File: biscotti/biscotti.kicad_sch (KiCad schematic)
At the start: 5 parts, among them U1 LAN8720A

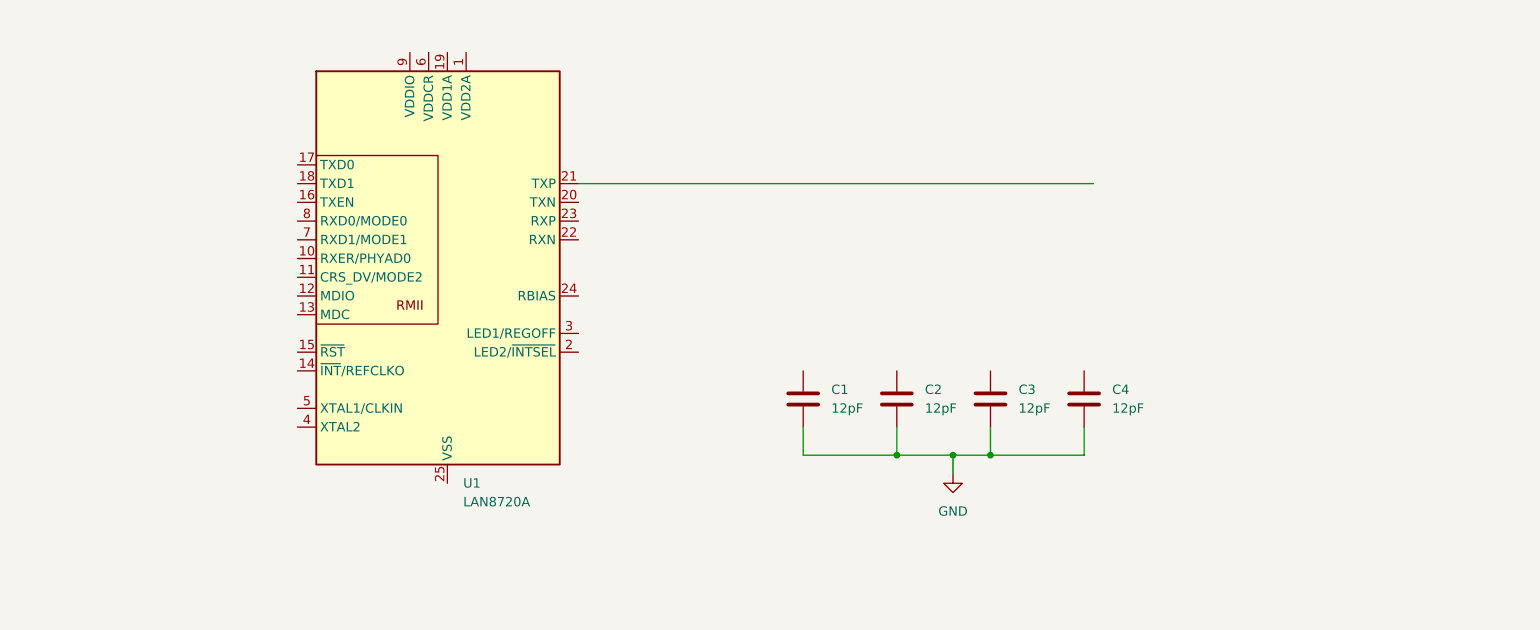
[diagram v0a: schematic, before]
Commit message: wip, started connected configs for LED1/2
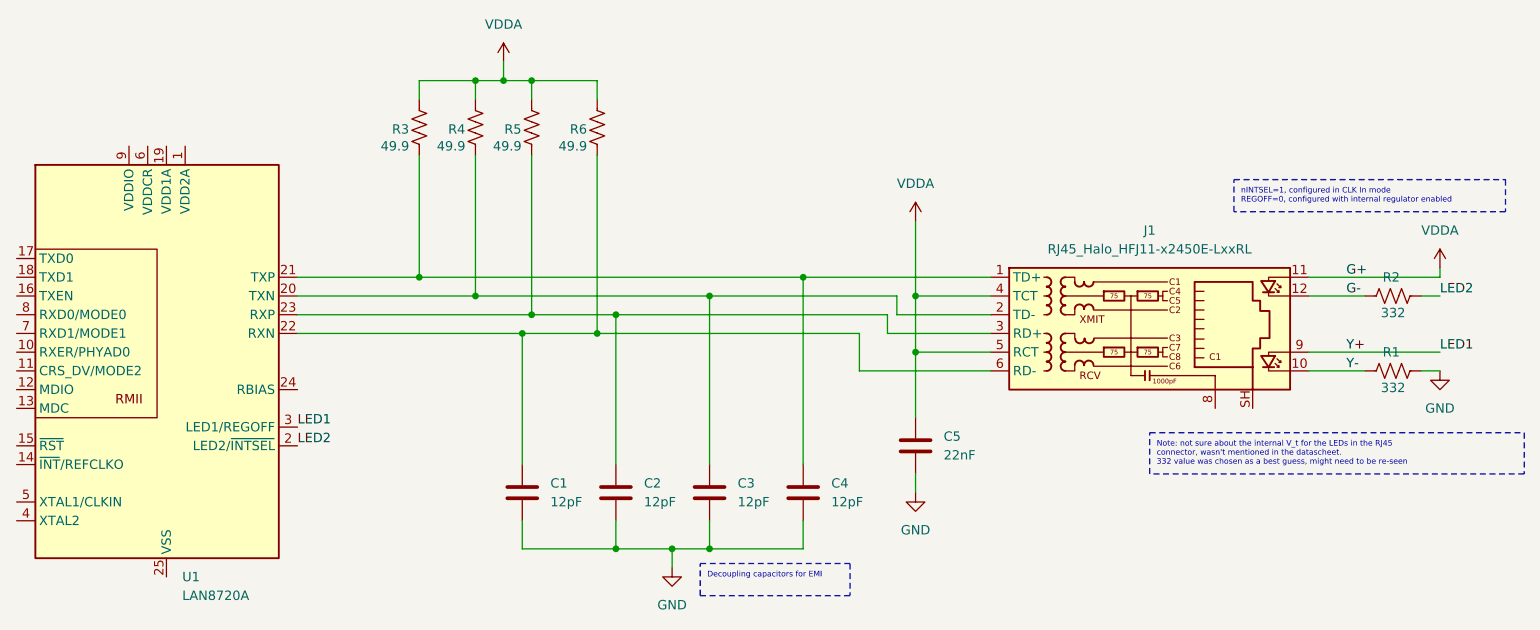
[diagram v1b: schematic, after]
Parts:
- added C5: 22nF, symbol Device:C
- added J1: RJ45_Halo_HFJ11-x2450E-LxxRL, Connector_RJ:RJ45_HALO_HFJ11-x2450E-LxxRL_Horizontal, symbol Connector:RJ45_Halo_HFJ11-x2450E-LxxRL
- added R1, R2: 332, symbol Device:R_US
- added R3, R4, R5, R6: 49.9, symbol Device:R_US
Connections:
- net GND: now also C5.2, R1.1
- net at C3.1: now also U1.20 (TXN), J1.2 (TD-), R4.2
- net at C1.1: now also U1.22 (RXN), J1.6 (RD-), R6.2
- net at C2.1: now also U1.23 (RXP), J1.3 (RD+), R5.2
- net at C4.1: now also U1.21 (TXP), J1.1 (TD+), R3.2
- net LED2: now reaches U1.2 (LED2/~{INTSEL})
- net LED2: now also R2.1
- net LED1: now reaches U1.3 (LED1/REGOFF)
- net LED1: now also J1.9
- new net G-: J1.12, R2.2
- new net VDDA: C5.1, J1.11, J1.4 (TCT), J1.5 (RCT), R3.1, R4.1, R5.1, R6.1
- new net Y-: J1.10, R1.2
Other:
- moved on the sheet: C1, C2, C3, C4, U1

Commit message: wip
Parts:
- added C6: 0.1uF, symbol Device:C
- added J2: Conn_02x06_Top_Bottom, symbol Connector_Generic:Conn_02x06_Top_Bottom
- added J3: Conn_02x01, symbol Connector_Generic:Conn_02x01
- added R7: 12.1k, symbol Device:R_US
- added R8: 1.5k, symbol Device:R_US
- added R9: 4.7k, symbol Device:R_US
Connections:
- net GND: now also U1.25 (VSS), C6.2, R7.2
- net MDIO: now reaches U1.12 (MDIO)
- net MDIO: now also J3.1 (Pin_1), R8.2
- net MDC: now reaches U1.13 (MDC)
- net MDC: now also J3.2 (Pin_2)
- net nRST: now reaches U1.15 (~{RST})
- net nRST: now also C6.1, R9.2
- net at U1.24 (RBIAS): now also R7.1
- net EGND: now reaches J1.8
- net EGND: now also J1.SH
- new net VDD: R8.1, R9.1
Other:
- note added: "EGND: copper pour around RJ45"
- note added: "This pin requires connection of a 12.1k ohm (1%) resistor to ground."

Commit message: add pmod
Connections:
- net GND: now also J2.11 (Pin_11), J2.5 (Pin_5)
- net Clk: now reaches J2.1 (Pin_1)
- net RXD[1]: now reaches J2.10 (Pin_10)
- net 3V3: now reaches J2.12 (Pin_12)
- net 3V3: now also J2.6 (Pin_6)
- net TXV: now reaches J2.2 (Pin_2)
- net RXV: now reaches J2.3 (Pin_3)
- net RXERR: now reaches J2.4 (Pin_4)
- net TXD[0]: now reaches J2.7 (Pin_7)
- net TXD[1]: now reaches J2.8 (Pin_8)
- net RXD[0]: now reaches J2.9 (Pin_9)

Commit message: config modes
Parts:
- added R10, R11, R12, R13: 4.7k, symbol Device:R_US
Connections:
- net GND: now also R12.2, R13.2
- net RXD[0]: now also U1.8 (RXD0/MODE0), R10.2
- net RXD[1]: now also U1.7 (RXD1/MODE1), R11.2
- net RXERR: now also U1.10 (RXER/PHYAD0), R13.1
- net RXV: now also U1.11 (CRS_DV/MODE2), R12.1
- net VDD: now also R10.1, R11.1
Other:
- note added: "MODE[2:0] = 011 100Base-TX Full Duplex. Auto-negotiation disabled. CRS is active during Receive MODE[0] 1 = RXD0/MODE0 MODE[1] 1 = RXD1/MODE1 MODE[2] 0 = CRS_DV/MODE2"

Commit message: finishing schematics and bom, next is routing
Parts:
- added C10, C12, C13, C7: 1uF, symbol Device:C
- added C11, C8, C9: 0.1uF, symbol Device:C
- added C14: 470pF, symbol Device:C
- added FB1: FerriteBead, symbol Device:FerriteBead
- added J4: Conn_01x01, symbol Connector_Generic:Conn_01x01
- added R14, R15, R16, R17: 10, symbol Device:R_US
- added R18: 4.7k, symbol Device:R_US
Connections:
- net Clk: now also U1.5 (XTAL1/CLKIN)
- net GND: now also C10.2, C11.2, C12.2, C13.2, C14.2, C7.2, C8.2, C9.2
- net RXD[0]: now also R14.1; no longer R10.2, U1.8 (RXD0/MODE0)
- net RXD[1]: now also R15.1; no longer R11.2, U1.7 (RXD1/MODE1)
- net RXERR: now also R16.1; no longer R13.1, U1.10 (RXER/PHYAD0)
- net RXV: now also R17.1; no longer R12.1, U1.11 (CRS_DV/MODE2)
- net TXD[0]: now also U1.17 (TXD0)
- net TXD[1]: now also U1.18 (TXD1)
- net TXV: now also U1.16 (TXEN)
- net VDD: now also U1.9 (VDDIO), C10.1, C9.1, FB1.2, R18.1
- net VDDA: now also U1.1 (VDD2A), U1.19 (VDD1A), C11.1, C12.1, C7.1, C8.1, FB1.1
- net nINT: now reaches U1.14 (~{INT}/REFCLKO)
- net nINT: now also J4.1 (Pin_1), R18.2
- net VDDCR: now reaches U1.6 (VDDCR)
- net VDDCR: now also C13.1, C14.1
- new net: R12.1, R17.2, U1.11 (CRS_DV/MODE2)
- new net: R10.2, R14.2, U1.8 (RXD0/MODE0)
- new net: R11.2, R15.2, U1.7 (RXD1/MODE1)
- new net: R13.1, R16.2, U1.10 (RXER/PHYAD0)
- no-connect marks 0 -> 1
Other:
- note added: "Bypass capacitors"
- note added: "nINT, interup, active low, exposed for debug"
- note added: "project_clk already has a 47 ohm resistor in series with the rpi pin (clock gen), so there is no need to add any more Rs on the line"
- moved on the sheet: C6, R12, R13, R9

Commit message: assign all footprints
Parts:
- C1, C10, C11, C12, C13, C14, C2, C3, C4, C5, C6, C7, C8, C9: footprint (none) -> Capacitor_SMD:C_1206_3216Metric_Pad1.33x1.80mm_HandSolder
- FB1: footprint (none) -> Inductor_SMD:L_1206_3216Metric_Pad1.22x1.90mm_HandSolder
- J2: footprint (none) -> Connector_PinHeader_2.54mm:PinHeader_2x06_P2.54mm_Horizontal
- J3: footprint (none) -> Connector_PinHeader_2.54mm:PinHeader_2x01_P2.54mm_Vertical
- J4: footprint (none) -> Connector_PinHeader_2.54mm:PinHeader_1x01_P2.54mm_Vertical
- R1, R10, R11, R12, R13, R14, R15, R16, R17, R18, R2, R3, R4, R5, R6, R7, R8, R9: footprint (none) -> Resistor_SMD:R_1206_3216Metric_Pad1.30x1.75mm_HandSolder
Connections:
- net 3V3 is gone; now on net VDD: J2.12 (Pin_12), J2.6 (Pin_6)

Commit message: placement in progress
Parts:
- removed J2: Conn_02x06_Top_Bottom, Connector_PinHeader_2.54mm:PinHeader_2x06_P2.54mm_Horizontal, symbol Connector_Generic:Conn_02x06_Top_Bottom
- added J2: Conn_02x06_Odd_Even, Connector_PinHeader_2.54mm:PinHeader_2x06_P2.54mm_Vertical, symbol Connector_Generic:Conn_02x06_Odd_Even
- renumbered C6 to C1, C8 to C10, C7 to C11, C5 to C12, C9 to C13, C10 to C14, C13 to C2, C14 to C3, C1 to C4, C2 to C5, C11 to C6, C3 to C7, C12 to C8, C4 to C9, J3 to J1, J4 to J3, J1 to J4, R8 to R1, R18 to R10, R9 to R11, R3 to R12, R7 to R13, R4 to R14, R5 to R15, R6 to R16, R2 to R17, R1 to R18, R14 to R2, R15 to R3, R16 to R4, R17 to R5, R10 to R6, R12 to R7, R11 to R8, R13 to R9
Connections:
- net Clk: now also J2.1 (Pin_1)
- net GND: now also J2.10 (Pin_10), J2.9 (Pin_9)
- net RXD[0]: now also J2.3 (Pin_3)
- net RXD[1]: now also J2.2 (Pin_2)
- net RXERR: now also J2.4 (Pin_4)
- net RXV: now also J2.5 (Pin_5)
- net TXD[0]: now also J2.8 (Pin_8)
- net TXD[1]: now also J2.7 (Pin_7)
- net TXV: now also J2.6 (Pin_6)
- net VDD: now also J2.11 (Pin_11), J2.12 (Pin_12)

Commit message: add artifacts
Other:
- company: (none) -> Julia Desmazes
- title: (none) -> Biscotti x1 PHY Ethernet Pmod
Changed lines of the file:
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@@
 	(generator_version "10.0")
 	(paper "A4")
+	(title_block
+		(title "Biscotti x1 PHY Ethernet Pmod")
+		(date "2026-07-26")
+		(rev "1.1")
+		(company "Julia Desmazes")
+	)
 	(text "This pin requires connection of a 12.1k ohm (1%)\nresistor to ground."
 		(exclude_from_sim no)
